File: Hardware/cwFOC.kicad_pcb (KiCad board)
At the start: 2 copper layers, 46 x 46 mm, 40 parts, among them J1 Motor, J2 Power, J4 Conn_01x06_MountingPin, J5 485, U1 MP6540, U2 AS5600, U3 HT7533, U5 MAX3485, U6 CW32F030K8

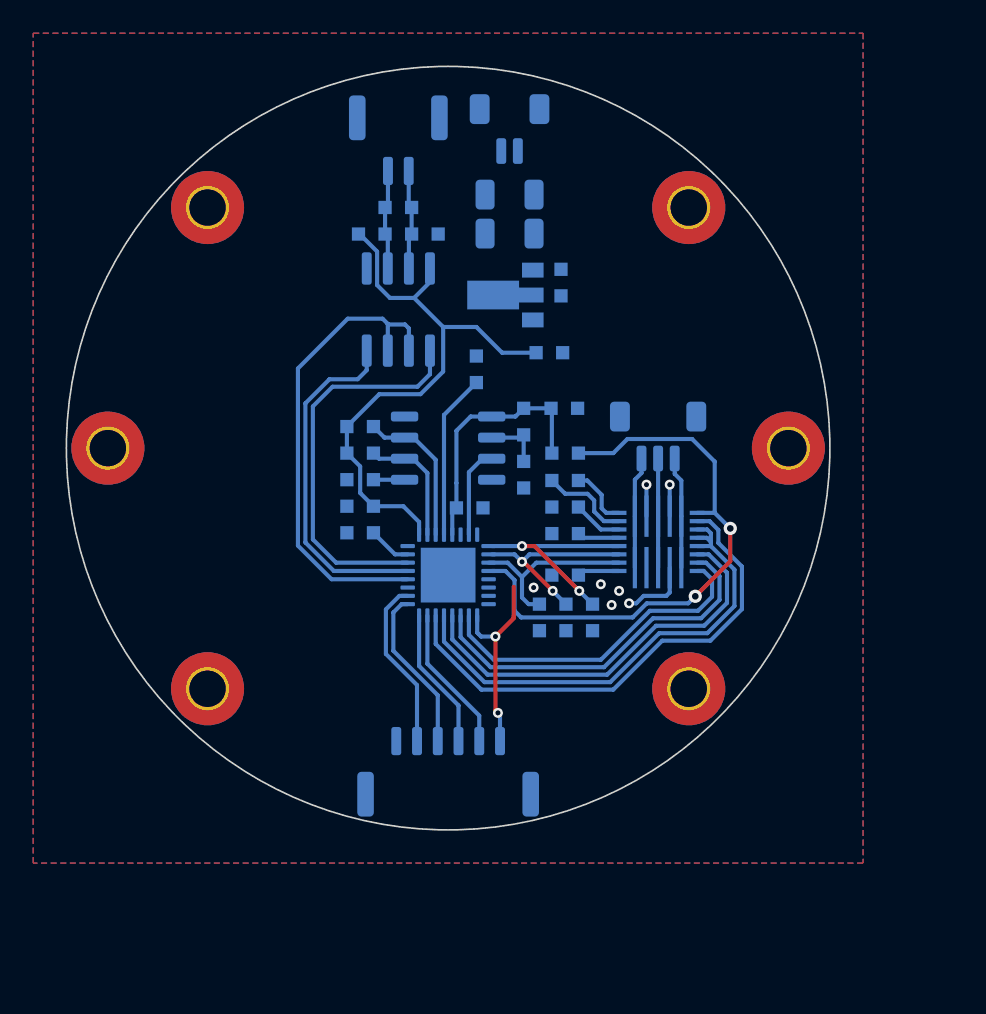
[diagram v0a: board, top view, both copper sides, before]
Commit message: 完成原理图设计，完成初步布局布线
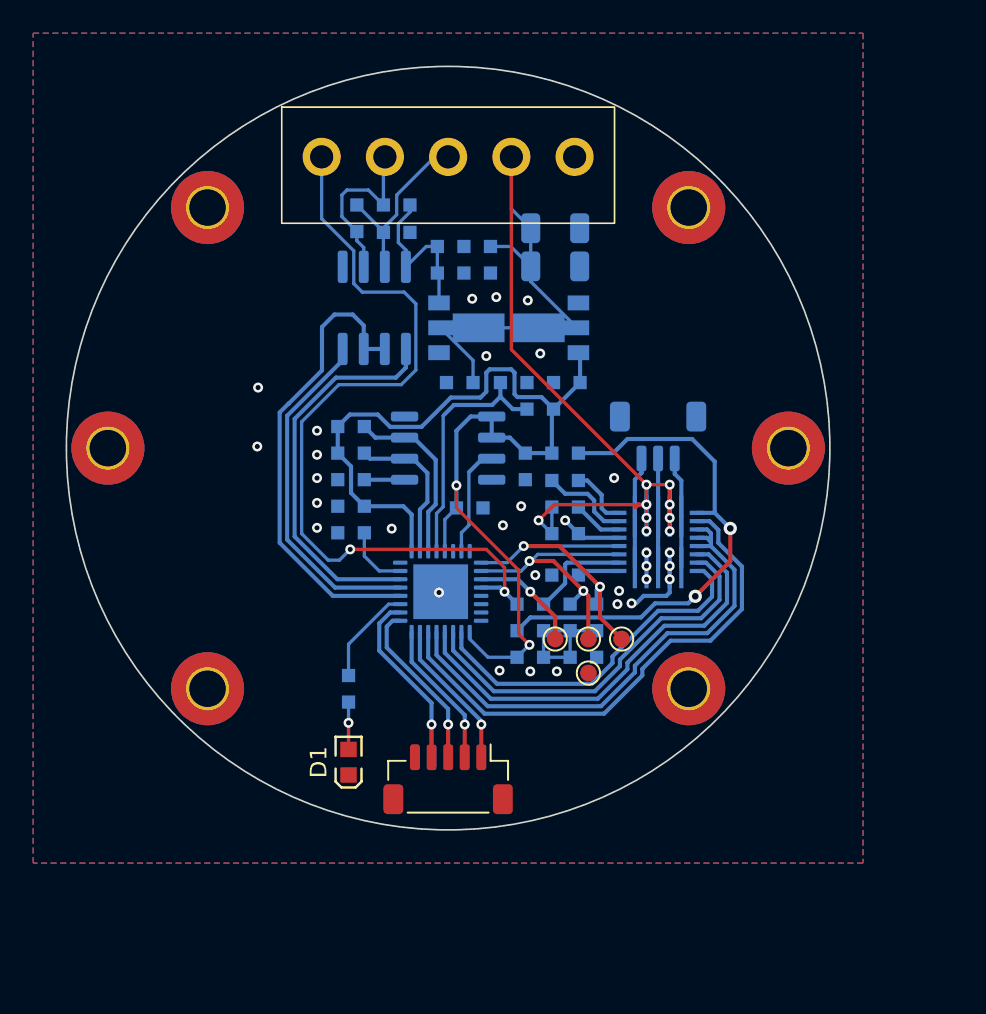
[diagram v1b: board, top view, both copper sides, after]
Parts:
- removed C4: 0.1uF, myDevice:0603_C
- removed J4: Conn_01x06_MountingPin, Connector_JST:JST_GH_SM06B-GHS-TB_1x06-1MP_P1.25mm_Horizontal
- removed J5: 485, Connector_JST:JST_GH_SM02B-GHS-TB_1x02-1MP_P1.25mm_Horizontal
- added C12: 1uF, myDevice:0603_C, B.Cu at (140.2, 77.8)
- added C3: 4.7uF, myDevice:0603_C, B.Cu at (140.7, 86.0)
- added C7: 4.7uF, myDevice:0603_C, B.Cu at (140.2, 79.5)
- added D1: LED, myDevice:0603_LED, F.Cu at (134.0, 108.9)
- added J3: KF2EDGV, myLib:KF2EDGV, F.Cu at (140.0, 72.5)
- added R11: 10K, myDevice:0603_R, B.Cu at (136.9, 77.0)
- added R12: 120R, myDevice:0603_R, B.Cu at (134.5, 76.2)
- added R8: 5K, myDevice:0603_R, B.Cu at (144.9, 102.6)
- added R9: 5K, myDevice:0603_R, B.Cu at (148.2, 102.6)
- added TP1: TestPoint, TestPoint:TestPoint_Pad_D1.0mm, F.Cu at (150.4, 101.5)
- added TP2: TestPoint, TestPoint:TestPoint_Pad_D1.0mm, F.Cu at (148.4, 101.5)
- added TP3: TestPoint, TestPoint:TestPoint_Pad_D1.0mm, F.Cu at (146.4, 101.5)
- added TP4: TestPoint, TestPoint:TestPoint_Pad_D1.0mm, F.Cu at (148.4, 103.5)
- added U4: HT7150, Package_TO_SOT_SMD:SOT-89-3, B.Cu at (141.4, 82.8)
- J2: value Power -> Debug; footprint Connector_JST:JST_SH_BM02B-SRSS-TB_1x02-1MP_P1.00mm_Vertical -> Connector_JST:JST_SH_BM05B-SRSS-TB_1x05-1MP_P1.00mm_Vertical; moved to F.Cu
- R10: value 0R -> 10K
- R14: value 120R -> 10K
- R16: value 10K -> 1K
- moved J2 39.3 mm to (140.0, 110.0)
- moved R16 27.4 mm to (134.0, 104.5), turned to 90 degrees
- moved R15 23.8 mm to (144.2, 100.2), turned to 90 degrees
- moved C15 4.47 mm to (142.6, 78.7), turned to -90 degrees
- moved C8 3.42 mm to (146.4, 76.8), turned to 0 degrees
- moved C9 3.39 mm to (146.4, 79.0), turned to 0 degrees
- moved U3 3.39 mm to (145.9, 82.8)
- moved C2 2.39 mm to (143.9, 86.0), turned to 180 degrees
- moved C16 2.08 mm to (147.2, 86.0), turned to 180 degrees
- moved U5 1.45 mm to (135.6, 81.5)
- moved R10 1.25 mm to (145.6, 87.7), turned to 0 degrees
- moved U6 1.10 mm to (139.6, 98.7)
- moved C21 0.55 mm to (134.2, 93.5)
- moved R2 0.55 mm to (134.2, 91.9)
- moved R3 0.55 mm to (134.2, 90.3)
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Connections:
- net /MCU/RS485_RXD renamed /MCU/UART2_RXD
- net /MCU/RS485_TXD renamed /MCU/UART2_TXD
- C6 pad 2: Net-(U2-VDD3V3) -> +3V3
- J2 pad 1: VBUS -> /MCU/SWDIO
- J2 pad 2: GND -> /MCU/SWCLK
- J2 pad MP: (no net) -> GND
- R1 pad 2: GND -> Net-(R1-Pad2)
- R10 pad 1: Net-(U2-VDD3V3) -> /MCU/nRST
- R14 pad 1: /MCU/B- -> /RS485/A+
- R14 pad 2: /MCU/A+ -> +5V
- R15 pad 1: GND -> /Driver/nFLT
- R15 pad 2: /MCU/B- -> BRK
- R16 pad 1: /MCU/A+ -> Net-(D1-A)
- R16 pad 2: +3V3 -> /MCU/LED
- R5 pad 2: GND -> Net-(R1-Pad2)
- R6 pad 2: GND -> Net-(R1-Pad2)
- U2 pad 2: Net-(U2-VDD3V3) -> +3V3
- U5 pad 6: /MCU/A+ -> /RS485/A+
- U5 pad 7: /MCU/B- -> /RS485/B-
- U5 pad 8: +3V3 -> +5V
- U6 pad 12: /Driver/nFLT -> BRK
- U6 pad 27: unconnected-(U6-PB4-Pad27) -> /MCU/LED
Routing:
- net VBUS: track 3.80 -> 71.3 mm, vias 2 -> 9
- net BRK: track 0.00 -> 49.2 mm, vias 0 -> 2
- net /RS485/B-: track 0.00 -> 11.1 mm
- net /RS485/A+: track 0.00 -> 10.8 mm
- net +5V: track 0.00 -> 10.0 mm
- net Net-(R1-Pad2): track 0.00 -> 8.00 mm
- net /MCU/B-: track 6.02 -> 0.00 mm
- net /MCU/A+: track 6.02 -> 0.00 mm
- net /MCU/LED: track 0.00 -> 6.00 mm
- net /Driver/SOC: track 13.4 -> 19.2 mm
- net /Driver/SOB: track 11.7 -> 16.9 mm
- net /MCU/nRST: track 9.97 -> 15.0 mm
- net Net-(U2-VDD3V3): track 3.59 -> 0.00 mm
- net /Driver/nFLT: track 34.6 -> 31.2 mm
- net /Driver/SOA: track 11.0 -> 14.1 mm, vias 0 -> 1
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
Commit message: 完善原理图设计、添加硬件README
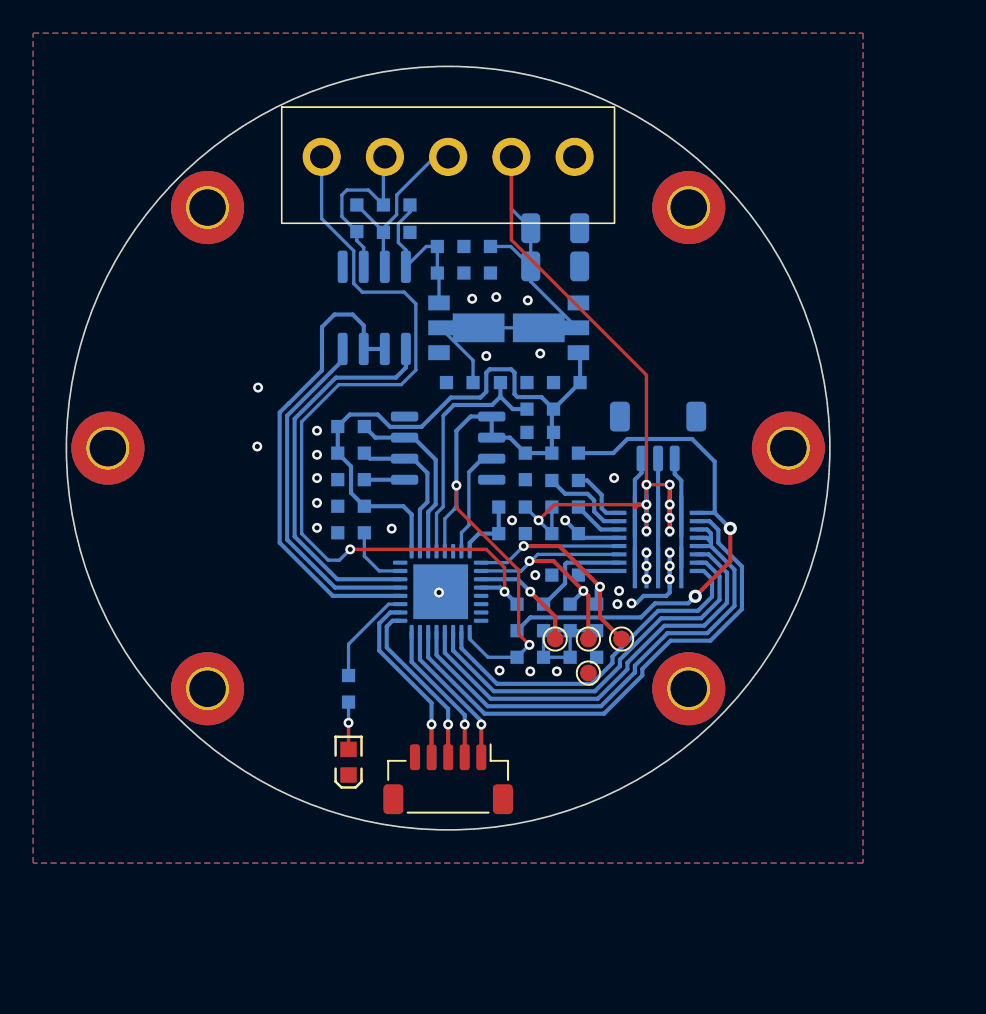
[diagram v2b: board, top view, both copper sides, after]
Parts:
- added R17: 5K, myDevice:0603_R, B.Cu at (143.8, 93.5)
- added R18: 1K, myDevice:0603_R, B.Cu at (143.8, 95.2)
- moved C23 6.23 mm to (145.6, 89.0)
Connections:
- U6 pad 8: unconnected-(U6-PA2-Pad8) -> /MCU/ADC_VBUS
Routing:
- net /MCU/ADC_VBUS: track 0.00 -> 4.09 mm
- net VBUS: track 71.3 -> 72.4 mm
- net GND: vias 31 -> 30

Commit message: 基本完成PCB设计
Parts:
- removed C15: 4.7uF, myDevice:0603_C
- added C4: 10uF, Capacitor_SMD:C_1206_3216Metric, B.Cu at (142.9, 78.4)
- added R19: 0R, myDevice:0603_R, B.Cu at (145.7, 69.7)
- C3: value 4.7uF -> 100nF
- H1, H2, H3, H4, H5, H6: footprint MountingHole:MountingHole_2.2mm_M2_Pad_TopBottom -> myLib:MountingHole_2.2mm_M2
- R15: value 10K -> 22R
- U2: footprint Package_SO:SOP-8_3.9x4.9mm_P1.27mm -> Package_SO:SOIC-8_3.9x4.9mm_P1.27mm
- moved C3 17.3 mm to (142.6, 103.3), turned to -90 degrees
- moved C2 3.83 mm to (140.2, 86.5), turned to 0 degrees
- moved R9 3.53 mm to (144.9, 104.1), turned to 180 degrees
- moved R10 2.48 mm to (143.3, 86.5)
- moved R16 2.08 mm to (132.3, 105.7)
- moved R7 2.02 mm to (132.3, 94.3), turned to -90 degrees
- moved U6 1.91 mm to (137.7, 98.8)
- moved R14 1.35 mm to (136.9, 76.7)
- moved R12 1.35 mm to (134.6, 77.5)
- moved R11 1.30 mm to (136.9, 78.3)
- moved U5 1.29 mm to (135.8, 82.8)
- moved TP4 0.95 mm to (147.5, 103.5)
- moved TP1 0.95 mm to (149.5, 101.5)
- moved TP2 0.95 mm to (147.5, 101.5)
- moved TP3 0.95 mm to (145.5, 101.5)
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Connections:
- net /MCU/UART2_RXD renamed /MCU/UART3_RXD
- net /MCU/UART2_TXD renamed /MCU/UART3_TXD
- C3 pad 1: VBUS -> +3V3
- C8 pad 2: GND -> GNDPWR
- C9 pad 2: GND -> GNDPWR
- J2 pad 1: /MCU/SWDIO -> GND
- J2 pad 2: /MCU/SWCLK -> /MCU/TXD
- J2 pad 4: /MCU/TXD -> /MCU/SWCLK
- J2 pad 5: GND -> /MCU/SWDIO
- J3 pad 5: GND -> GNDPWR
- U1 pad 10: GND -> GNDPWR
- U1 pad 12: GND -> GNDPWR
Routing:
- net VBUS: track 72.4 -> 33.2 mm, vias 9 -> 7
- net GND: track 7.95 -> 14.9 mm, vias 30 -> 42
- net GNDPWR: track 0.00 -> 6.91 mm, vias 0 -> 8
- net +3V3: track 66.5 -> 70.3 mm
- net /Driver/SOA: track 14.1 -> 17.8 mm, vias 1 -> 2
- net /Driver/ENA: track 31.0 -> 34.7 mm
- net /MCU/RXD: track 10.4 -> 14.0 mm
- net /MCU/TXD: track 10.9 -> 14.5 mm
- net /MCU/SWCLK: track 8.86 -> 12.1 mm
- net /MCU/SWDIO: track 9.07 -> 12.4 mm
- net /Driver/SOC: track 19.2 -> 22.4 mm
- net /Driver/SOB: track 16.9 -> 20.1 mm
- net BRK: track 49.2 -> 51.9 mm
- net /Driver/nSLP: track 31.5 -> 34.2 mm
- net +5V: track 10.0 -> 7.48 mm
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- added copper zone on B.Cu, net GNDPWR
- added copper zone on F.Cu, net GNDPWR
- added copper zone on B.Cu, net VBUS
- added copper zone on F.Cu, net VBUS

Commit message: 第一版硬件做好啦！(●'◡'●)
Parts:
- added REF**: OSHW-Logo2_7.3x6mm_SilkScreen, Symbol:OSHW-Logo2_7.3x6mm_SilkScreen, F.Cu at (125.5, 83.0)
- added REF**: ESD-Logo_6.6x6mm_SilkScreen, Symbol:ESD-Logo_6.6x6mm_SilkScreen, B.Cu at (125.5, 82.5)
- added REF**: WEEE-Logo_4.2x6mm_SilkScreen, Symbol:WEEE-Logo_4.2x6mm_SilkScreen, B.Cu at (153.7, 83.5)
- added REF**: KiCad-Logo2_5mm_SilkScreen, Symbol:KiCad-Logo2_5mm_SilkScreen, B.Cu at (126.0, 93.3)
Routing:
- net VBUS: track 33.2 -> 37.0 mm, vias 7 -> 9
- net GND: vias 42 -> 131
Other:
- board text added: "12V"
- board text added: "A"
- board text added: "A+"
- board text added: "B"
- board text added: "B-"
- board text added: "BRK"
- board text added: "C"
- board text added: "CLK"
- board text added: "DIO"
- board text added: "G"
- board text added: "GND"
- board text added: "JLCJLCJLCJLC"
- board text added: "RXD"
- board text added: "TXD"

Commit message: 调整第二版原理图
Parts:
- removed REF**: OSHW-Logo2_7.3x6mm_SilkScreen, Symbol:OSHW-Logo2_7.3x6mm_SilkScreen
- removed REF**: ESD-Logo_6.6x6mm_SilkScreen, Symbol:ESD-Logo_6.6x6mm_SilkScreen
- removed REF**: WEEE-Logo_4.2x6mm_SilkScreen, Symbol:WEEE-Logo_4.2x6mm_SilkScreen
- removed REF**: KiCad-Logo2_5mm_SilkScreen, Symbol:KiCad-Logo2_5mm_SilkScreen
- added C13: 10pF, myDevice:0603_C, F.Cu at (135.6, 95.5)
- added C14: 10pF, myDevice:0603_C, F.Cu at (135.6, 97.1)
- added C15: 10pF, myDevice:0603_C, F.Cu at (135.6, 98.7)
- added D2: SMAJ15CA, Diode_SMD:D_SMA, F.Cu at (148.1, 87.8)
- added D3: SMAJ15CA, Diode_SMD:D_SMA, F.Cu at (151.6, 87.8)
- added D4: SMAJ15CA, Diode_SMD:D_SMA, F.Cu at (155.1, 87.8)
- added D5: SS54, Diode_SMD:D_SMB, F.Cu at (168.2, 80.3)
- added R20: 22R, myDevice:0603_R, B.Cu at (138.8, 98.7)
- added R21: 22R, myDevice:0603_R, B.Cu at (138.8, 97.1)
- added R22: 22R, myDevice:0603_R, B.Cu at (138.8, 95.5)
- J2: value Debug -> Conn_01x06_MountingPin; footprint Connector_JST:JST_SH_BM05B-SRSS-TB_1x05-1MP_P1.00mm_Vertical -> Connector_JST:JST_GH_SM06B-GHS-TB_1x06-1MP_P1.25mm_Horizontal
- R1, R5, R6: moved to F.Cu
- moved C10 23.2 mm to (164.1, 113.5)
- moved C11 23.1 mm to (164.5, 110.4)
- moved R15 20.1 mm to (153.8, 117.7)
- moved R9 20.1 mm to (154.6, 121.7)
- moved R8 20.1 mm to (154.6, 120.1)
- moved C3 20.1 mm to (152.2, 120.9)
- moved R13 17.7 mm to (148.0, 108.0)
- moved U1 12.1 mm to (142.9, 102.8), turned to 90 degrees
- moved R1 8.33 mm to (142.0, 95.5), turned to 180 degrees
- moved R5 6.13 mm to (142.0, 97.1), turned to 180 degrees
- moved C5 6.09 mm to (141.6, 95.9), turned to -90 degrees
- moved C1 5.77 mm to (143.9, 96.7)
- moved U6 4.65 mm to (133.0, 98.6)
- moved R6 4.00 mm to (142.0, 98.7), turned to 180 degrees
- moved R7 2.20 mm to (132.3, 92.1)
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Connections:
- C11 pad 1: VBUS -> VIN
- C5 pad 1: VBUS -> VIN
- J2 pad 1: GND -> /MCU/SWDIO
- J2 pad 2: /MCU/TXD -> /MCU/SWCLK
- J2 pad 4: /MCU/SWCLK -> /MCU/TXD
- J2 pad 5: /MCU/SWDIO -> /MCU/nRST
- U1 pad 15: /Driver/SOA -> Net-(U1-SOA)
- U1 pad 16: /Driver/SOB -> Net-(U1-SOB)
- U1 pad 17: /Driver/SOC -> Net-(U1-SOC)
- U1 pad 23: VBUS -> VIN
- U1 pad 25: VBUS -> VIN
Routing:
- net +3V3: track 70.5 -> 0.00 mm, vias 2 -> 0
- net BRK: track 51.9 -> 0.00 mm, vias 2 -> 0
- net VBUS: track 37.0 -> 0.00 mm, vias 9 -> 0
- net /Driver/nFLT: track 29.2 -> 0.00 mm, vias 2 -> 0
- net /MCU/RS485_DIR: track 26.3 -> 0.00 mm
- net /Driver/SOC: track 22.4 -> 0.00 mm, vias 2 -> 0
- net /MCU/UART3_RXD: track 21.5 -> 0.00 mm
- net /Driver/SOB: track 20.1 -> 0.00 mm, vias 2 -> 0
- net /MCU/UART3_TXD: track 18.6 -> 0.00 mm
- net /Driver/SOA: track 17.8 -> 0.00 mm, vias 2 -> 0
- net /Driver/nSLP: track 34.1 -> 18.7 mm
- net /Driver/ENA: track 34.7 -> 19.4 mm
- net GND: track 14.9 -> 0.00 mm, vias 131 -> 0
- net /MCU/TXD: track 14.5 -> 0.00 mm, vias 1 -> 0
- net /Driver/PWMA: track 28.6 -> 14.6 mm
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- removed copper zone on B.Cu, net GND
- removed copper zone on F.Cu, net GND
- removed copper zone on B.Cu, net GNDPWR
- removed copper zone on F.Cu, net GNDPWR
- removed copper zone on B.Cu, net VBUS
- removed copper zone on F.Cu, net VBUS

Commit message: 小修小补，拉了点线
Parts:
- removed R2: 0R, myDevice:0603_R
- removed TP1, TP2, TP3, TP4: TestPoint, TestPoint:TestPoint_Pad_D1.0mm
- removed U4: HT7150, Package_TO_SOT_SMD:SOT-89-3
- added D6: D_TVS, Diode_SMD:D_SMA, F.Cu at (145.7, 78.3)
- R1, R5, R6: moved to B.Cu
- R15: value 22R -> 470R
- moved R9 31.4 mm to (138.5, 94.7)
- moved C3 28.7 mm to (136.1, 97.1), turned to 90 degrees
- moved R8 28.5 mm to (141.7, 94.7), turned to 180 degrees
- moved R15 27.3 mm to (146.9, 91.3), turned to 180 degrees
- moved C11 26.1 mm to (144.5, 93.7), turned to 90 degrees
- moved D5 25.8 mm to (143.1, 86.3)
- moved C10 24.7 mm to (145.3, 97.5)
- moved R13 18.3 mm to (146.9, 89.7)
- moved U1 12.5 mm to (153.0, 95.4), turned to 180 degrees
- moved R17 9.06 mm to (141.1, 84.9)
- moved R18 9.06 mm to (141.1, 86.5)
- moved C7 7.70 mm to (146.6, 79.9)
- moved R12 6.36 mm to (139.6, 76.6), turned to 180 degrees
- moved C14 6.15 mm to (141.7, 97.9), turned to 180 degrees
- moved C13 6.15 mm to (141.7, 96.3), turned to 180 degrees
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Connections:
- C12 pad 1: +5V -> +3V3
- C4 pad 2: GND -> GNDPWR
- C7 pad 1: +5V -> VBUS
- R14 pad 2: +5V -> +3V3
- U2 pad 5: Net-(U2-PGO) -> unconnected-(U2-PGO-Pad5)
- U5 pad 8: +5V -> +3V3
- U6 pad 7: /Encoder/OUT -> unconnected-(U6-PA1-Pad7)
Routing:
- net +3V3: track 0.00 -> 66.9 mm, vias 0 -> 2
- net BRK: track 0.00 -> 45.1 mm
- net /MCU/RS485_DIR: track 0.00 -> 29.2 mm
- net /MCU/UART3_TXD: track 0.00 -> 22.6 mm
- net /Driver/nSLP: track 18.7 -> 40.7 mm
- net /Driver/PWMA: track 14.6 -> 35.7 mm
- net /Driver/PWMB: track 13.1 -> 33.6 mm
- net /Driver/PWMC: track 11.5 -> 31.5 mm
- net /MCU/nRST: track 0.00 -> 19.2 mm
- net /MCU/SWDIO: track 0.00 -> 18.9 mm
- net /MCU/TXD: track 0.00 -> 18.4 mm
- net /Driver/ENA: track 19.4 -> 37.7 mm
- net /MCU/UART3_RXD: track 0.00 -> 18.2 mm
- net /MCU/SWCLK: track 0.00 -> 18.0 mm
- net /MCU/RXD: track 0.00 -> 17.2 mm
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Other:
- board text removed: "A"
- board text removed: "B"
- board text removed: "C"
- board text removed: "CLK"
- board text removed: "DIO"
- board text removed: "G"
- board text removed: "RXD"
- board text removed: "TXD"

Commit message: 完成第二版硬件
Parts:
- removed C9: 10uF, Capacitor_SMD:C_1206_3216Metric
- added D7: SMAJ15CA, Diode_SMD:D_SMA, F.Cu at (135.1, 78.3)
- H1, H2, H3, H4, H5, H6: value MountingHole_Pad -> MountingHole; moved to F.Cu
- R3, R4: value 4.7K -> 2.2K
- moved H5 40.9 mm to (125.6, 104.4), turned to 0 degrees
- moved H2 40.9 mm to (154.4, 75.6), turned to 0 degrees
- moved H3 15.7 mm to (160.5, 90.0), turned to 0 degrees
- moved H6 15.7 mm to (119.5, 90.0), turned to 0 degrees
- moved H1 15.6 mm to (125.6, 75.6), turned to 0 degrees
- moved H4 15.6 mm to (154.4, 104.4), turned to 0 degrees
- moved D2 3.54 mm to (149.5, 83.6)
- moved D3 3.54 mm to (153.0, 83.6)
- moved D4 3.54 mm to (156.5, 83.6)
- moved D5 3.54 mm to (145.5, 83.7)
- moved R11 2.55 mm to (138.7, 80.9)
- moved R14 2.55 mm to (137.1, 80.9)
- moved U5 2.55 mm to (132.6, 80.4)
- moved R12 2.55 mm to (137.9, 78.5)
- moved C12 2.55 mm to (137.9, 83.3)
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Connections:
- J2 pad 1: /MCU/SWDIO -> GND
- J2 pad 2: /MCU/SWCLK -> /MCU/nRST
- J2 pad 3: /MCU/RXD -> /MCU/TXD
- J2 pad 4: /MCU/TXD -> /MCU/RXD
- J2 pad 5: /MCU/nRST -> /MCU/SWCLK
- J2 pad 6: GND -> /MCU/SWDIO
- J3 pad 1: BRK -> /RS485/A+
- J3 pad 2: /RS485/A+ -> /RS485/B-
- J3 pad 3: /RS485/B- -> BRK
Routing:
- net /MCU/nRST: track 19.2 -> 39.2 mm, vias 0 -> 1
- net GNDPWR: track 0.00 -> 14.3 mm, vias 0 -> 4
- net VBUS: track 0.00 -> 14.2 mm
- net /RS485/B-: track 0.00 -> 12.7 mm
- net /RS485/A+: track 0.00 -> 11.8 mm
- net /Driver/SOA: track 5.53 -> 15.8 mm
- net BRK: track 45.1 -> 35.2 mm
- net +3V3: track 66.9 -> 75.9 mm, vias 2 -> 4
- net /Driver/SOB: track 6.67 -> 14.8 mm
- net /Driver/SOC: track 6.68 -> 13.9 mm
- net VIN: track 8.23 -> 15.0 mm
- net /MCU/RXD: track 17.2 -> 21.9 mm, vias 0 -> 1
- net /Driver/W: track 13.7 -> 9.42 mm
- net GND: track 8.89 -> 12.6 mm, vias 6 -> 80
- net /MCU/TXD: track 18.4 -> 21.8 mm, vias 0 -> 1
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- added copper zone on F.Cu, net /Driver/U
- added copper zone on F.Cu, net /Driver/V
- added copper zone on F.Cu, net /Driver/W
- added copper zone on F.Cu, net /RS485/A+
- added copper zone on F.Cu, net /RS485/B-
- added copper zone on B.Cu, net GND
- added copper zone on F.Cu, net GND
- added copper zone on B.Cu, net GNDPWR
- added copper zone on F.Cu, net GNDPWR
- added copper zone on B.Cu, net VBUS
- added copper zone on F.Cu, net VBUS
- added copper zone on F.Cu, net VIN
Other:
- board text added: "GND 12V BRK B- A+"
- board text added: "GND nRST TXD RXD CLK DIO"
- board text added: "cwFOC Rev 2.0 2023/04/12"
- board text removed: "12V"
- board text removed: "A+"
- board text removed: "B-"
- board text removed: "BRK"
- board text removed: "GND"
